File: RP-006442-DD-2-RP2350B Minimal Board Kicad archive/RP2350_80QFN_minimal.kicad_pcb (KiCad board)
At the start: 2 copper layers, 100 x 100 mm, 129 parts, among them J1 USB_C_Receptacle_USB2.0_16P, J2 Conn_02x20_Odd_Even, J3 Conn_02x09_Odd_Even, J4 Conn_01x03, J5 USB_C_Receptacle_USB2.0_16P, SW1 SW_Push, SW10 SW_DIP_x08, SW11 SW_Omron_B3FS, SW12 SW_Omron_B3FS, SW13 SW_Omron_B3FS, SW14 SW_Omron_B3FS, SW2 SW_Push, SW3 SW_Push, SW4 SW_Push, U1 RP2350_80QFN, U10 74HC595, U11 74HC595, U2 NCP1117-3.3_SOT223, U3 W25Q128JVS, U4 DNF, U5 W25Q128JVS, U6 NCP1117-3.3_SOT223, U7 RP2350_60QFN, U8 HT16K33A-24SSOP, U9 CC56-12EWA, Y1 ABM8-272-T3, Y2 ABM8-272-T3

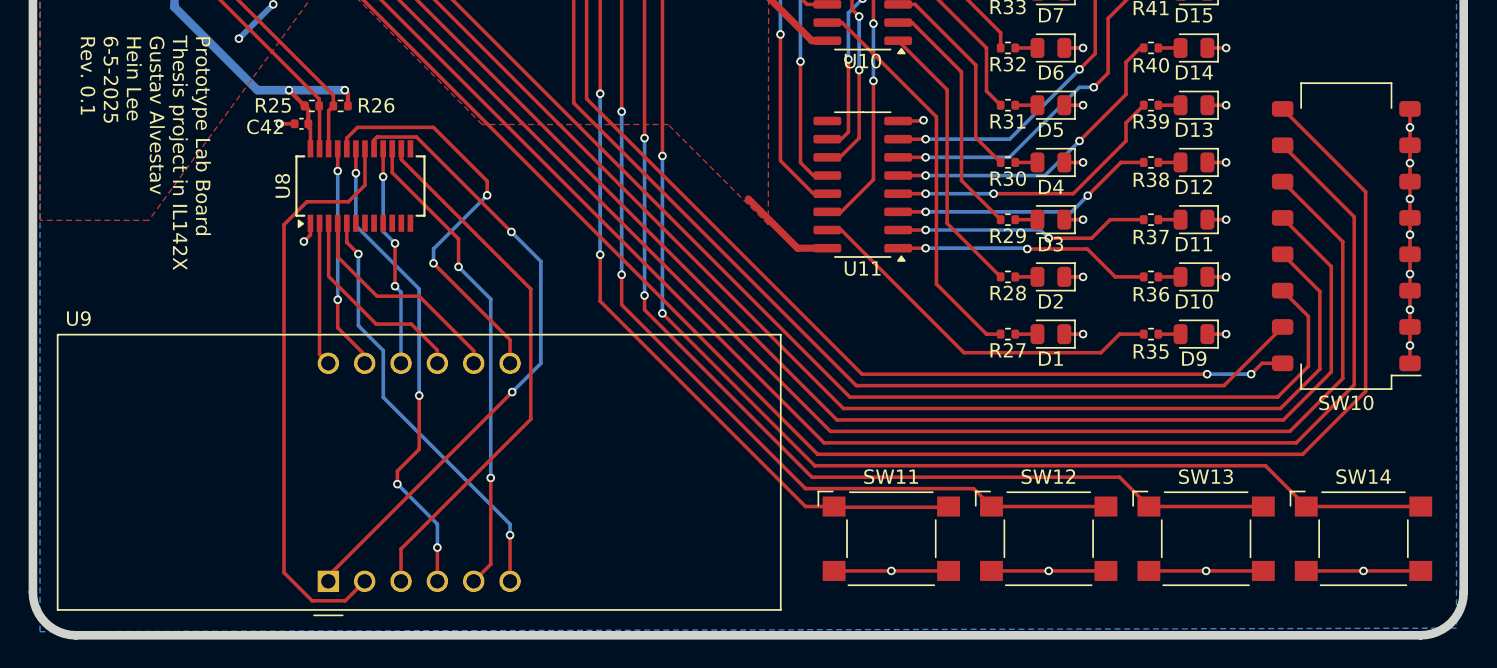
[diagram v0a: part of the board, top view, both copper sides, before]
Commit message: Update RP2350_80QFN_minimal.kicad_pcb
moved hex display outside of 5mm of pcb edge
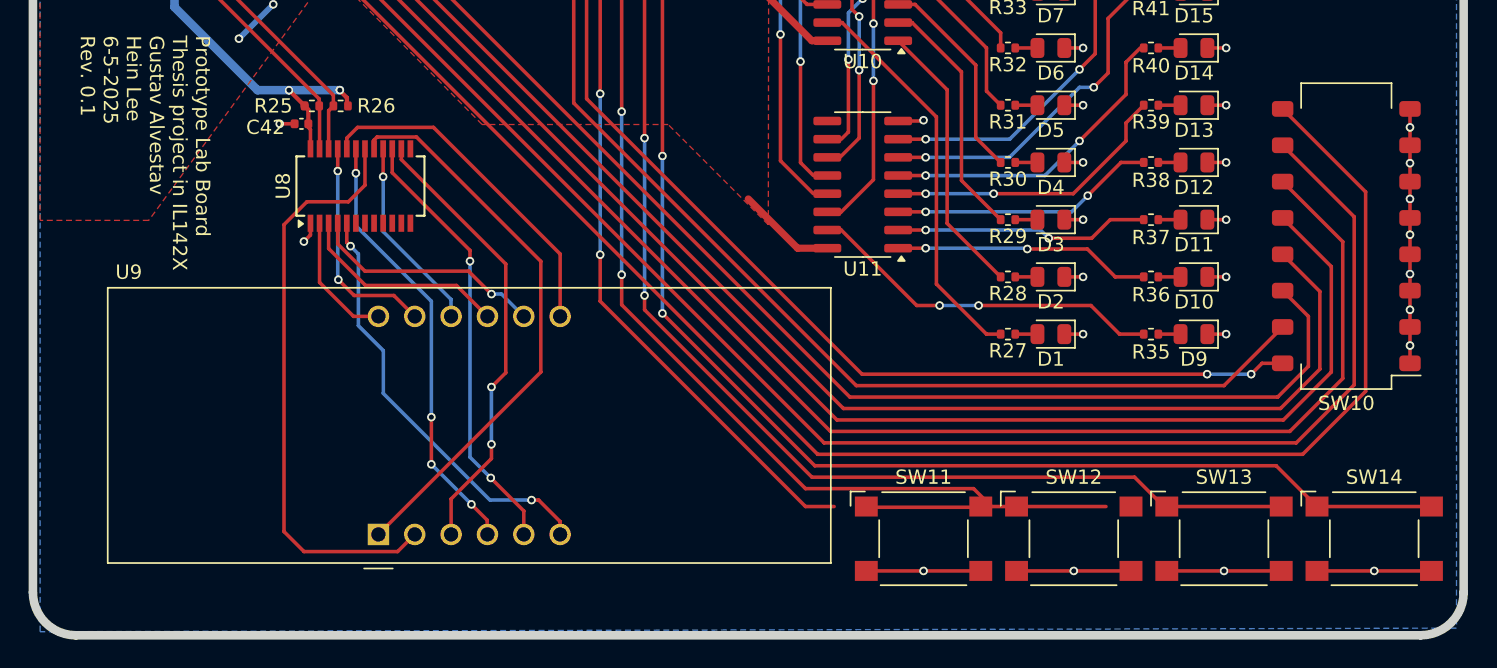
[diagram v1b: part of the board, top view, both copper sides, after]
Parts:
- moved U9 4.79 mm to (86.0, 138.0)
- moved SW11 2.25 mm to (124.1, 138.3)
- moved SW12 1.75 mm to (134.6, 138.3)
- moved SW13 1.25 mm to (145.1, 138.3)
- moved SW14 0.75 mm to (155.6, 138.3)
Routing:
- net /Hex displays peripheral/ROW7: track 37.7 -> 31.6 mm, vias 0 -> 2
- net /Hex displays peripheral/ROW4: track 44.8 -> 39.7 mm, vias 2 -> 0
- net /Hex displays peripheral/ROW1: track 28.9 -> 24.0 mm, vias 2 -> 0
- net /Hex displays peripheral/ROW2: track 33.9 -> 30.8 mm
- net /Hex displays peripheral/ROW6: track 33.6 -> 30.8 mm
- net /Hex displays peripheral/ROW5: track 15.5 -> 13.7 mm, vias 3 -> 1
- net /Hex displays peripheral/COM2: track 15.5 -> 16.6 mm, vias 0 -> 1
- net /LEDs/D9: track 26.2 -> 25.1 mm, vias 0 -> 2
- net /GPIO32: track 101.5 -> 102.6 mm
- net /Hex displays peripheral/COM0: track 10.0 -> 9.23 mm
- net /GPIO33: track 114.3 -> 115.0 mm

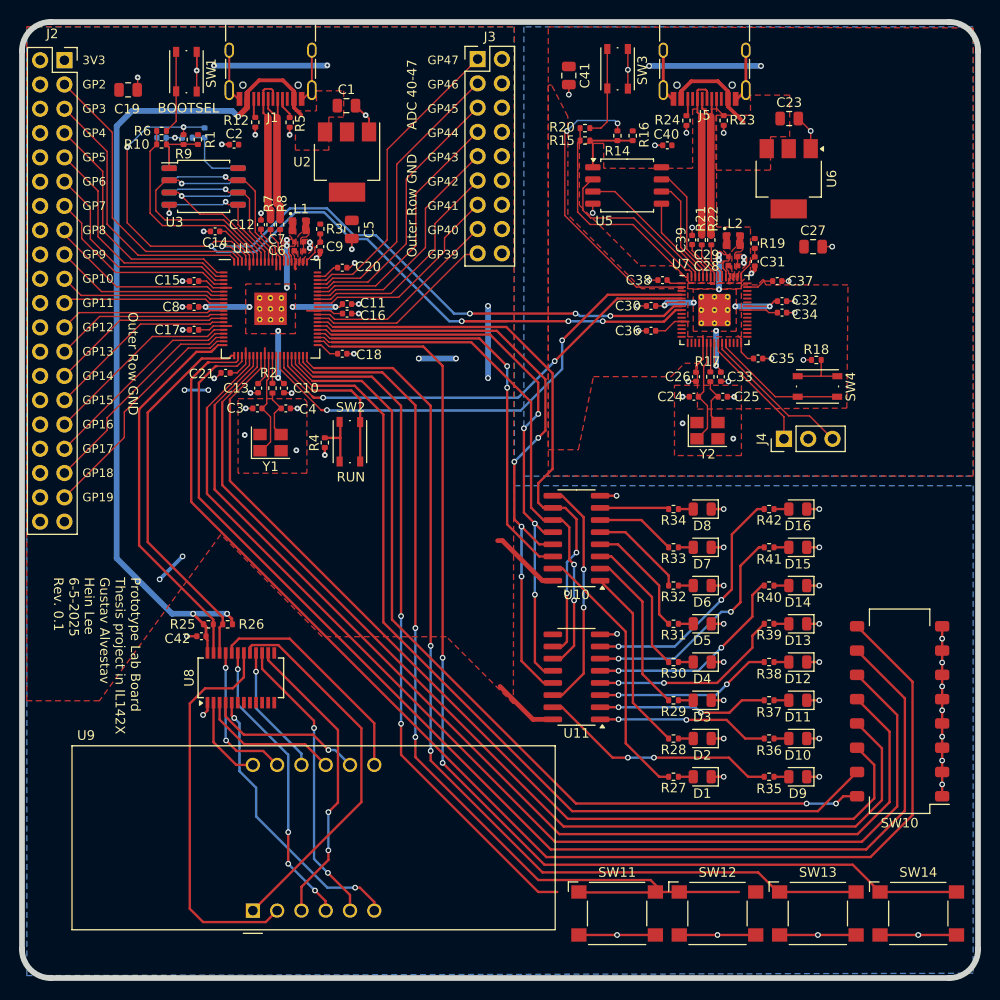
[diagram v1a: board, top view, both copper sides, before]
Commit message: Update RP2350_80QFN_minimal.kicad_pcb
Fixed some DRC errors
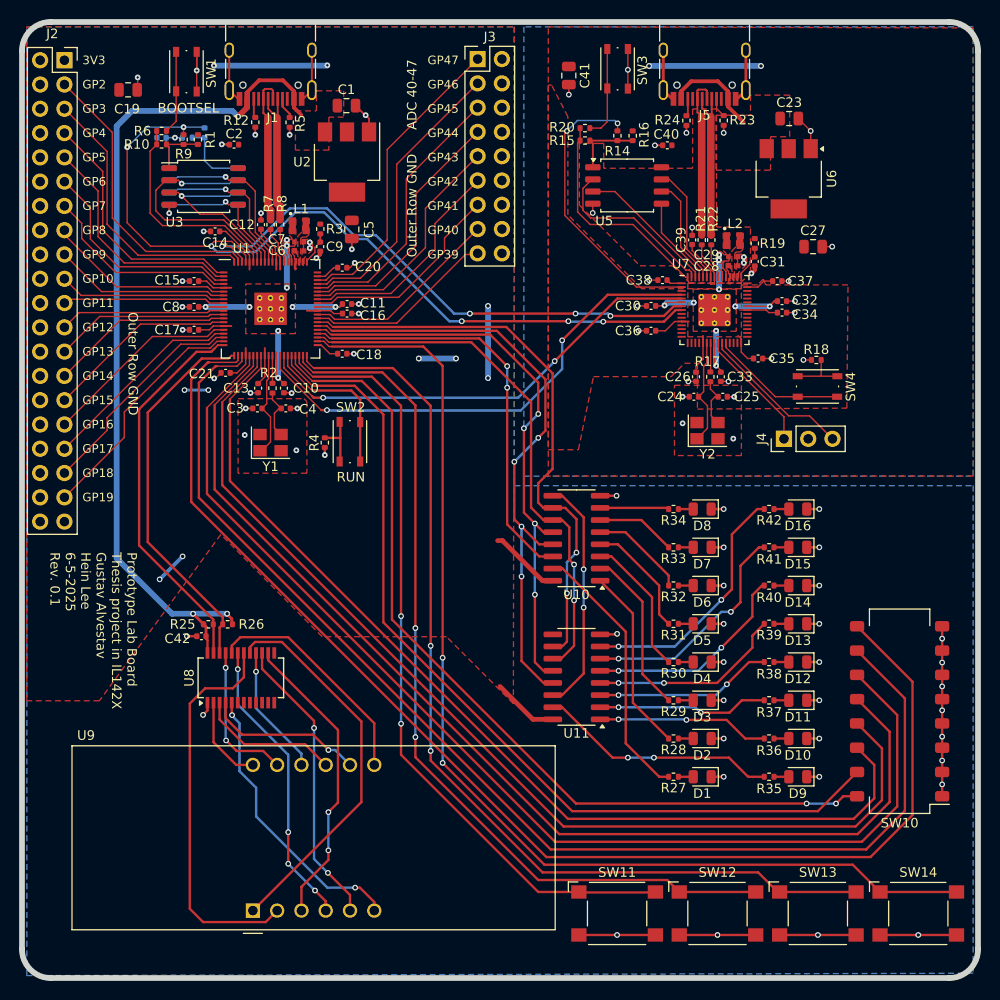
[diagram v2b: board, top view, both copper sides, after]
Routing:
- net /GPIO0: track 98.5 -> 89.2 mm
- net /GPIO30: track 80.1 -> 82.3 mm
- net /GPIO31: track 90.8 -> 92.6 mm
- net /Hex displays peripheral/ROW4: track 39.7 -> 40.4 mm

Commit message: Update RP2350_80QFN_minimal.kicad_pcb
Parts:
- J2: value Conn_02x20_Odd_Even -> Conn_02x19_Odd_Even; footprint Connector_PinSocket_2.54mm:PinSocket_2x20_P2.54mm_Vertical -> Connector_PinSocket_2.54mm:PinSocket_2x19_P2.54mm_Vertical
- moved J2 0.07 mm to (66.3, 49.0)
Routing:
- net /GPIO0: track 89.2 -> 88.7 mm

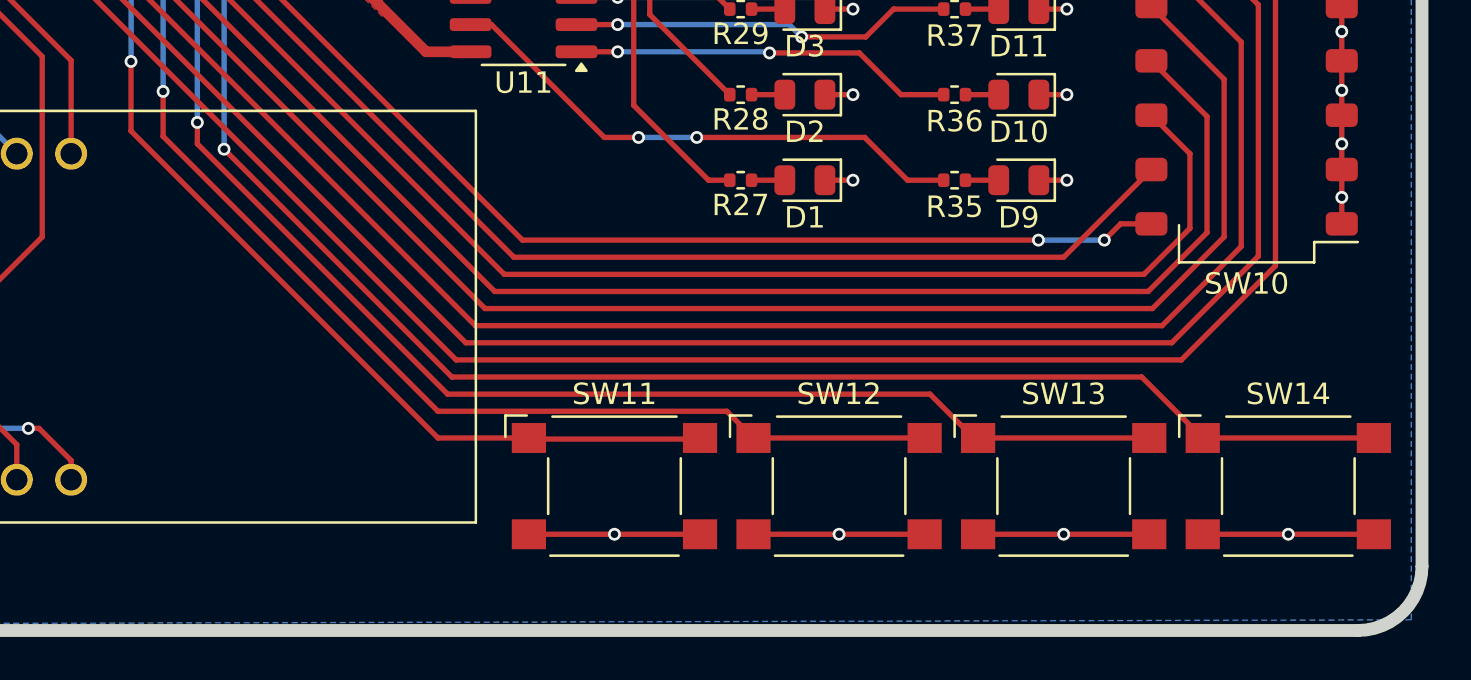
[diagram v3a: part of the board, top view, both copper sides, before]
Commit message: Update pushbutton footprints on pcb
Changed from omron pushbutton footprints to custom footprints for JLCPCB part
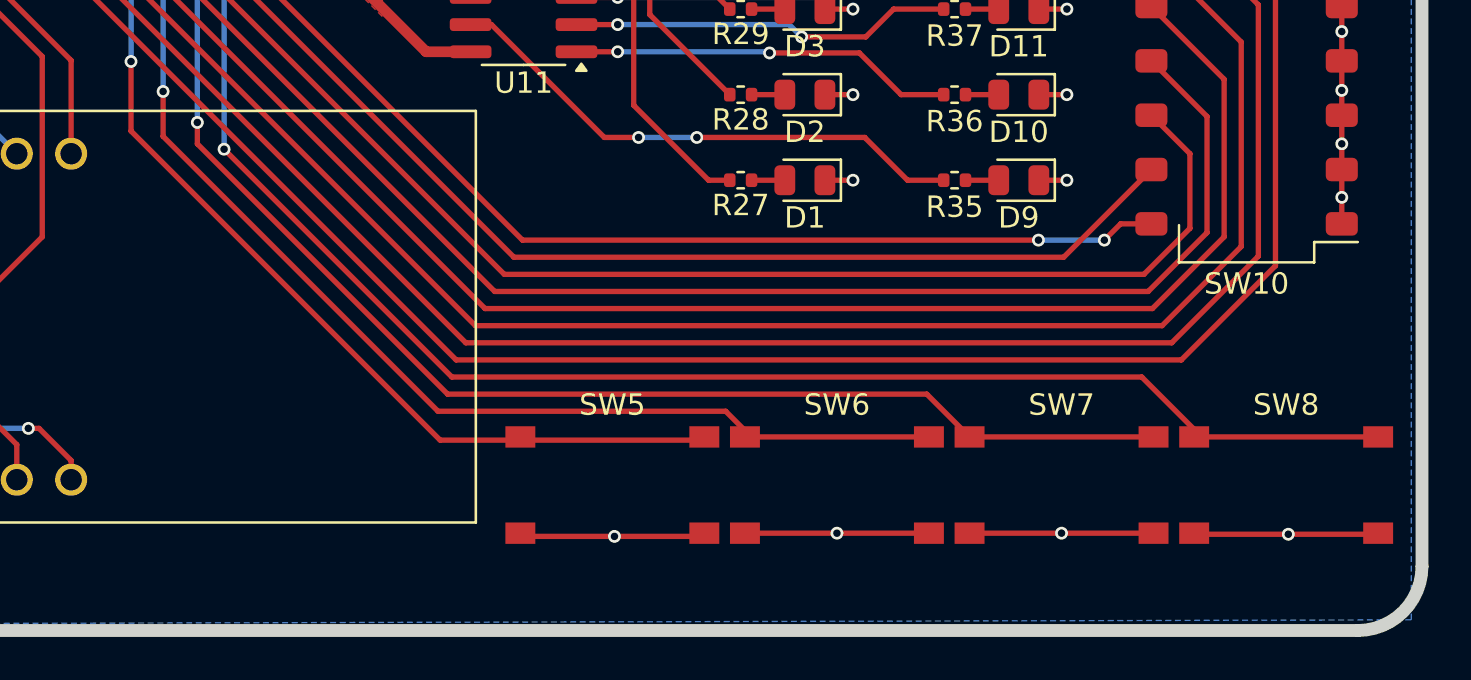
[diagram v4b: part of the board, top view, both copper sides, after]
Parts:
- removed SW11, SW12, SW13, SW14: SW_Omron_B3FS, Button_Switch_SMD:SW_SPST_Omron_B3FS-100xP
- added SW5: SW_Push, Button_Switch_SMD:SW_Push_K2-1102SP-A4SC-04, F.Cu at (119.0, 135.5)
- added SW6: SW_Push, Button_Switch_SMD:SW_Push_K2-1102SP-A4SC-04, F.Cu at (129.5, 135.5)
- added SW7: SW_Push, Button_Switch_SMD:SW_Push_K2-1102SP-A4SC-04, F.Cu at (140.0, 135.5)
- added SW8: SW_Push, Button_Switch_SMD:SW_Push_K2-1102SP-A4SC-04, F.Cu at (150.5, 135.5)
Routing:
- net GND: track 152.2 -> 153.8 mm
- net /GPIO30: track 82.3 -> 82.9 mm

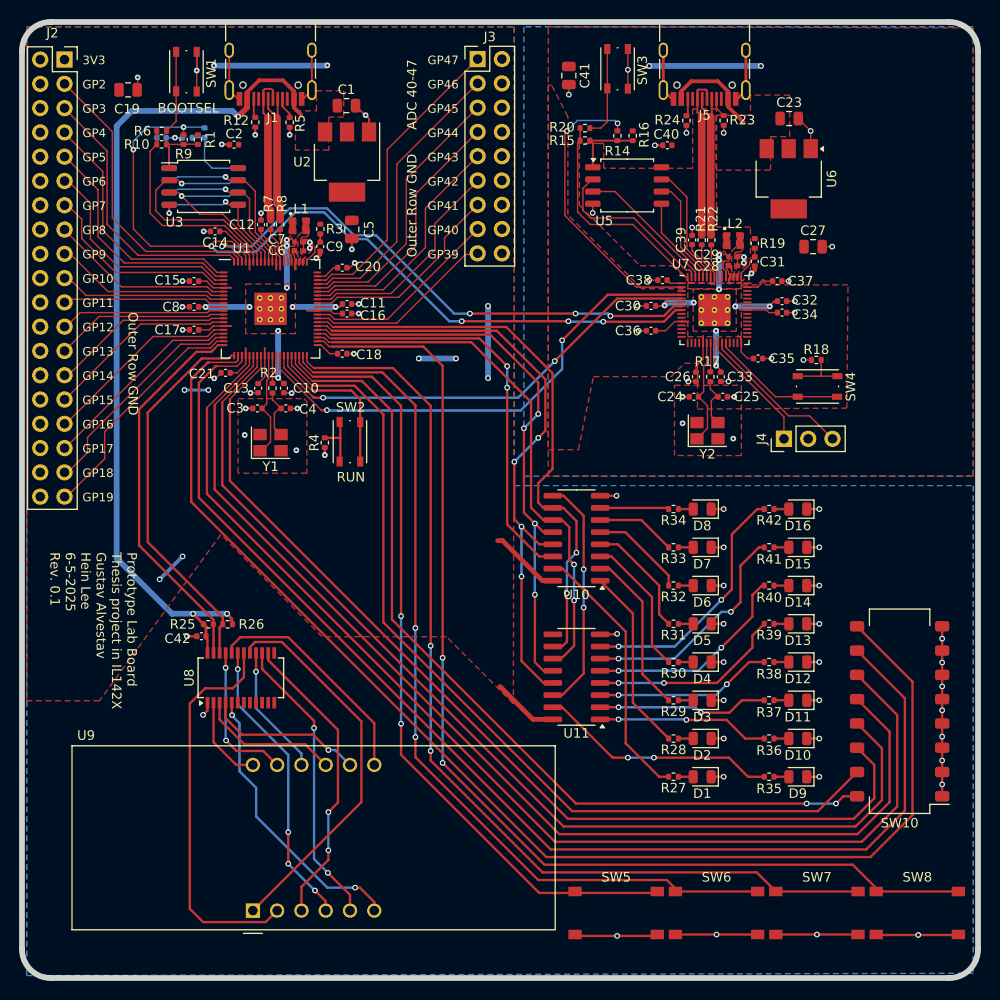
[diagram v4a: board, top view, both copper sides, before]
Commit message: Update to schematic and pcb
Changed:
- Added 100n decoupling capacitors to both 74HC595
- Changed ground plane to single common ground plane
- Added schottky diode to usb vbus inputs, creating separate vbus and vsys
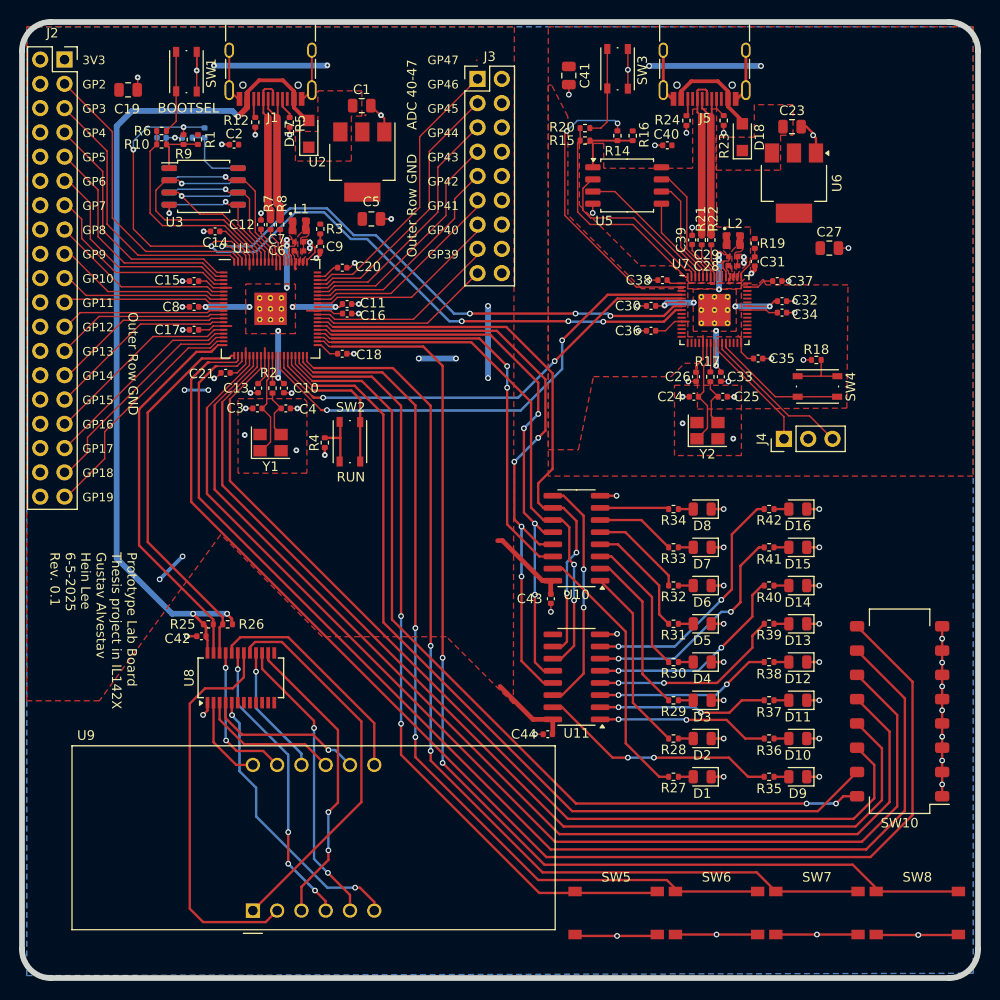
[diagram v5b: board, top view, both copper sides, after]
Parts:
- added C43: 100n, Capacitor_SMD:C_0402_1005Metric, F.Cu at (117.2, 105.4)
- added C44: 100n, Capacitor_SMD:C_0402_1005Metric, F.Cu at (116.8, 119.5)
- added D17: PMEG6010ELR, Diode_SMD:Nexperia_CFP3_SOD-123W, F.Cu at (91.8, 56.8)
- added D18: PMEG6010ELR, Diode_SMD:Nexperia_CFP3_SOD-123W, F.Cu at (137.2, 57.1)
- moved C5 2.33 mm to (98.4, 65.7), turned to 0 degrees
- moved J3 2.07 mm to (109.5, 51.0)
- moved C27 1.71 mm to (146.3, 68.7)
- moved C1 1.60 mm to (97.4, 53.8)
- moved U2 1.60 mm to (97.5, 59.7)
- moved C23 0.90 mm to (142.4, 56.0)
- moved U6 0.71 mm to (142.6, 61.9)
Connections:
- C1 pad 1: VBUS -> VDC
- C23 pad 1: VBUS -> VDC
- U2 pad 3: VBUS -> VDC
- U6 pad 3: VBUS -> VDC
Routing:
- net +3V3: track 125.7 -> 128.7 mm
- net /GPIO43_ADC3: track 25.1 -> 23.1 mm
- net /GPIO45_ADC5: track 28.4 -> 26.5 mm
- net /GPIO44_ADC4: track 26.7 -> 24.8 mm
- net /GPIO46_ADC6: track 30.1 -> 28.2 mm
- net /GPIO42_ADC2: track 23.4 -> 21.5 mm
- net /GPIO47_ADC7: track 31.8 -> 29.9 mm
- net GND: track 153.8 -> 155.5 mm, vias 85 -> 87
- net VBUS: track 100.9 -> 102.0 mm
- net /GPIO41_ADC1: track 21.7 -> 20.6 mm
- net /GPIO39: track 19.9 -> 19.1 mm
- added copper zone on F.Cu, net VDC
- removed copper zone on F.Cu, net VBUS

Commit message: Update
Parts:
- added J6: Conn_01x05, Connector_PinHeader_2.54mm:PinHeader_1x05_P2.54mm_Vertical, F.Cu at (118.8, 71.5)
- moved C41 1.90 mm to (121.0, 50.6)
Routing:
- net VDC: track 0.06 -> 35.5 mm, vias 0 -> 2
- net /GPIO1: track 57.8 -> 59.0 mm, vias 4 -> 3
- net /SWD: track 48.5 -> 49.1 mm
- net /SWCLK: track 64.8 -> 65.5 mm, vias 2 -> 1
- net /GPIO0: track 88.7 -> 88.8 mm, vias 6 -> 5
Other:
- board text added: "GND"
- board text added: "GPIO0"
- board text added: "GPIO1"
- board text added: "SWCLK"
- board text added: "SWD"
